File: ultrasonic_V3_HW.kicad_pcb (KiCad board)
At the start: 4 copper layers, 130 x 100 mm, 249 parts, among them J1 71918-140LF, J2 Conn_Coaxial, J3 Conn_Coaxial, J4 Conn_01x07_Pin, J5 Screw_Terminal_01x02, J6 Conn_Coaxial, J7 Conn_Coaxial, Q1 DMN6069SE, Q10 DMN6069SE, Q11 DMN6069SE, Q15 NMOS, Q2 DMN6069SE, Q3 DMN6069SE, Q4 DMN6069SE, Q5 NMOS, Q6 NMOS, Q7 DMN6069SE, Q8 DMN6069SE, Q9 DMN6069SE, U1 MACHXO2-1200HC-4TG100C, U10 MIC4604YM, U11 MIC4604YM, U12 OKI-78SR-3.3_1.5-W36H-C, U13 OKI-78SR-12_1.0-W36H-C, U15 LM34966, U17 OPA388, U18 LM393, U2 TDC_7200, U23 MCP1501-25xCH, U24 MCP1501-30xCH, U3 MAX9939, U4 TLV3501AID, U5 DGS0010A, U6 LM339, U7 ADC10065, U8 MIC4604YM, U9 MIC4604YM, X1 16MHz

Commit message: DONE - before checking
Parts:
- added R83: 12, Resistor_SMD:R_0603_1608Metric, B.Cu at (126.9, 92.0)
- added R84: 12, Resistor_SMD:R_0603_1608Metric, B.Cu at (126.9, 93.5)
- added R85: 12, Resistor_SMD:R_0603_1608Metric, B.Cu at (126.9, 95.0)
- C1, C12, C61: value 100p -> C
- C10, C11, C13, C14, C18, C20, C21, C22, C23, C24, C25, C3, C35, C38, C39, C41, C42, C44, C45, C47, C48, C50, C51, C52, C54, C63, C7, C78, C79, C8, C80, C81, C82, C83, C84, C85, C88, C89, C9: value 100n -> C
- C15, C62, C64, C65, C68, C69, C71, C73, C75, C77: value 4u7 -> C
- C16, C17, C5, C6, C66, C67, C70, C72, C74, C76, C86, C87: value 220n -> C
- C19: value 4.7u -> C
- C26, C28, C31, C32, C36, C37, C40, C43, C46, C49, C53, C60: value 1u -> C
- C27, C29, C30, C33, C4, C58: value 10n -> C
- C34, C55: value 1n -> C
- C56: value 220p -> C
- C57, C59: value 22n -> C
- D1, D2, D3, D5, D6: value 1N4148W -> D
- D24, D26, D27: value LED_GREEN -> LED
- D4: value V8PA6HM3/I -> D
- L2: value 6.8u -> L
- R1, R10, R11, R12, R13, R15, R16, R17, R18, R19, R2, R21, R24, R25, R3, R4, R51, R6, R72, R73, R74, R75, R82, R9: value 0 -> R
- R14, R23, R52, R60, R62, R63, R64, R65: value 100 -> R
- R20, R22, R26, R27, R28, R42, R43, R44, R45, R46, R47, R5, R58, R59, R61, R66, R67, R68, R69, R70, R71, R76, R77, R78, R79, R8, R80, R81: value 10k -> R
- R48: value 6k8 -> R
- R49: value 11k3 -> R
- R50: value 49k9 -> R
- R53, R54: value 10m -> R
- R7: value 1k -> R
- U19, U20, U21, U22: value ~ -> TMUX7219
- moved C14 4.82 mm to (182.7, 94.6), turned to -90 degrees
- moved C85 3.83 mm to (168.1, 69.1)
- moved R19 3.79 mm to (165.4, 92.4), turned to 0 degrees
- moved U24 3.75 mm to (167.1, 69.2), turned to 90 degrees
- moved R24 3.22 mm to (159.1, 87.6), turned to 180 degrees
- moved R15 2.81 mm to (162.4, 87.6), turned to 0 degrees
- moved R21 1.97 mm to (168.8, 92.4), turned to 0 degrees
- moved C54 1.30 mm to (165.3, 76.3)
- moved C55 1.30 mm to (165.3, 74.8)
- moved C53 1.30 mm to (165.1, 73.0)
- moved C18 1.20 mm to (165.9, 87.6)
- moved C13 0.86 mm to (156.7, 90.8), turned to 90 degrees
- moved C79 0.70 mm to (92.5, 81.3)
- moved C7 0.60 mm to (160.8, 94.1)
- moved C26 0.40 mm to (96.4, 98.2)
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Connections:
- U1 pad 10: /SPI_LOCAL_MOSI -> Net-(U1D-PL4B)
- U1 pad 12: /SPI_LOCAL_SCK -> Net-(U1D-PL5A/PCLKT3_1)
- U1 pad 9: /SPI_LOCAL_MISO -> Net-(U1D-PL4A)
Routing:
- net GND: track 253.4 -> 230.9 mm, vias 117 -> 393
- net /SPI_LOCAL_SCK: track 116.4 -> 109.2 mm, vias 5 -> 4
- net /SPI_LOCAL_MOSI: track 117.0 -> 109.9 mm, vias 4 -> 3
- net /SPI_LOCAL_MISO: track 10.9 -> 4.89 mm, vias 2 -> 1
- net Net-(U1D-PL5A/PCLKT3_1): track 0.00 -> 4.69 mm, vias 0 -> 1
- net Net-(U1D-PL4B): track 0.00 -> 4.40 mm, vias 0 -> 1
- net Net-(U1D-PL4A): track 0.00 -> 4.33 mm, vias 0 -> 1
- net Net-(U17A-+): track 12.3 -> 16.4 mm
- net /P3V_REF: track 39.6 -> 35.7 mm
- net /H-bridges/BRIDGE_CD_MUX_EN: track 82.6 -> 80.7 mm
- net /CNTRL_GPIO2: track 86.8 -> 88.5 mm, vias 2 -> 3
- net /CNTRL_GPIO3: track 33.6 -> 35.1 mm, vias 0 -> 1
- net /CNTRL_MOSI: track 47.3 -> 48.9 mm, vias 2 -> 3
- net /CNTRL_GPIO1: track 33.8 -> 35.0 mm, vias 0 -> 1
- net /CNTRL_SCLK: track 49.1 -> 50.3 mm, vias 2 -> 3
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- added copper zone on B.Cu, net GND
- added copper zone on F.Cu, net GND

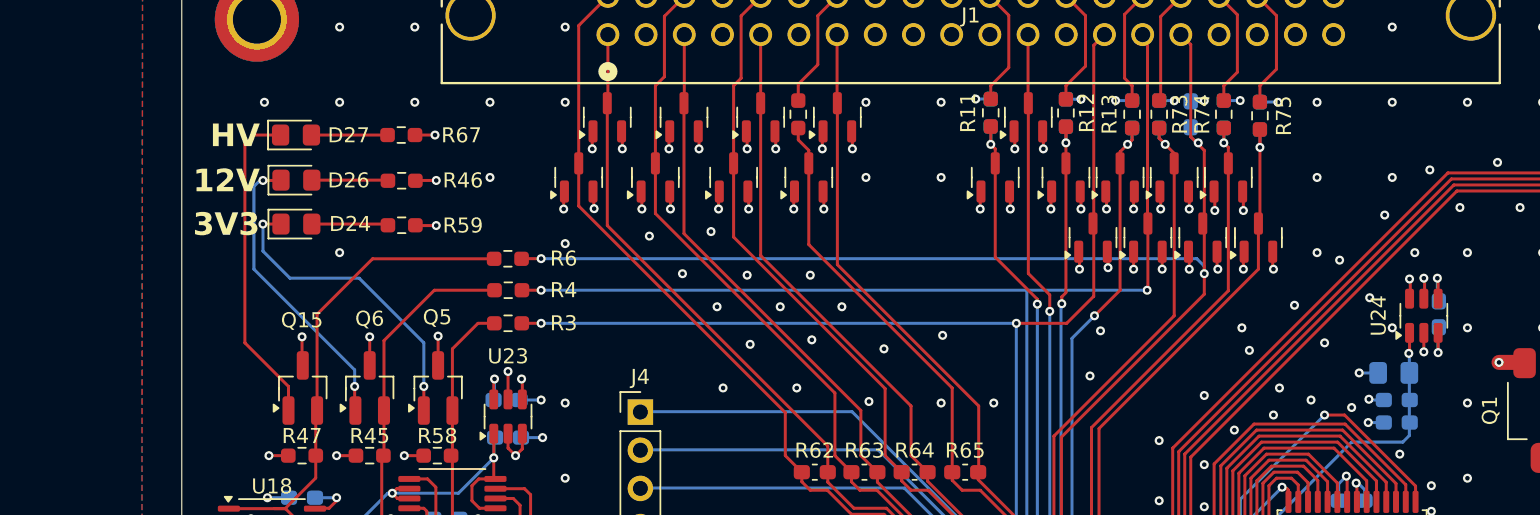
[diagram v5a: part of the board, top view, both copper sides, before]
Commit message: most values in schematic filled corrected footprint mistake
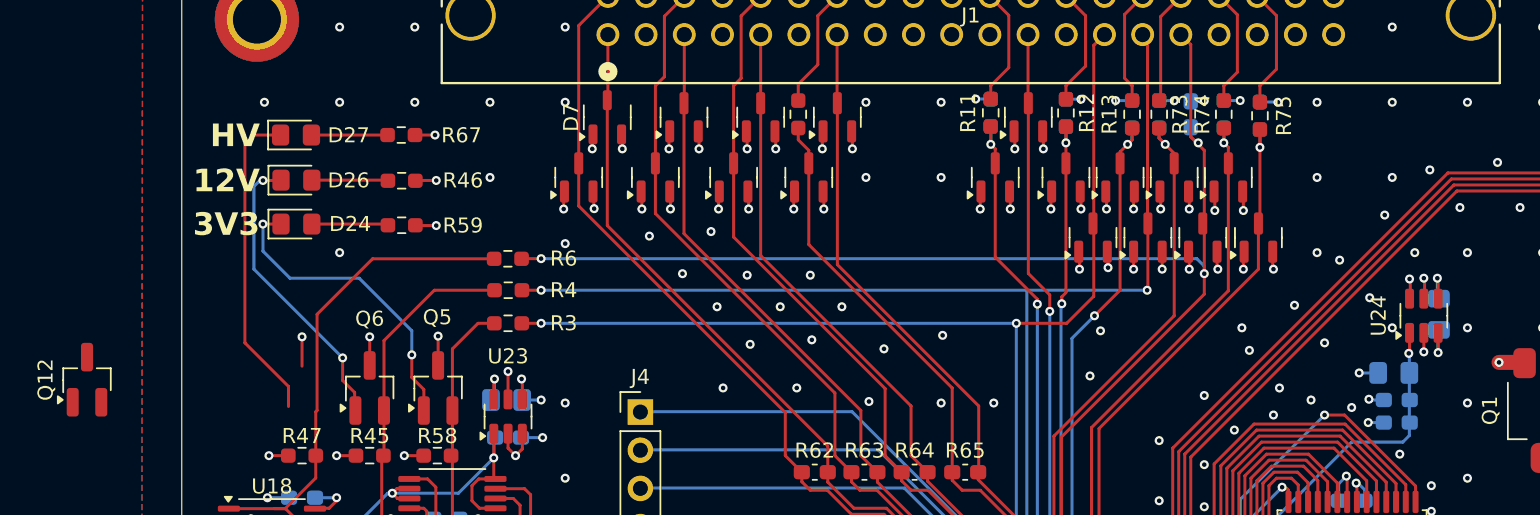
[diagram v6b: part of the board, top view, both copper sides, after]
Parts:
- removed Q15: NMOS, Package_TO_SOT_SMD:SOT-23_Handsoldering
- added Q12: Q_NMOS_GSD, Package_TO_SOT_SMD:SOT-23_Handsoldering, F.Cu at (78.2, 73.5)
- C1, C12, C61: value C -> 100p
- C10, C11, C53, C60: value C -> 1u
- C13, C14, C27, C29, C30, C33, C54, C58, C63, C7, C78, C79, C80, C89, C9: value C -> 100n
- C15, C26, C28, C31, C32, C62: value C -> 10u
- C55: value C -> 10n
- C56: value C -> 220p
- C57: value C -> 22n
- C59: value C -> 220n
- C85, C88: value C -> 1u; footprint Capacitor_SMD:C_0603_1608Metric_Pad1.08x0.95mm_HandSolder -> Capacitor_SMD:C_0805_2012Metric_Pad1.18x1.45mm_HandSolder
- D4: value D -> V8PA6HM3/I
- D7: footprint Package_TO_SOT_SMD:SOT-23 -> Package_TO_SOT_SMD:SOT-23-3
- L2: value L -> 6.8u
- Q5, Q6: value NMOS -> Q_NMOS_GSD
- R11, R12, R13, R18, R3, R4, R51, R6, R72, R73, R74, R75, R82: value R -> 0
- R16, R17, R19, R21, R46, R59, R67: value R -> 1k
- R22: value R -> 8k2
- R45, R47, R5, R58, R8: value R -> 10k
- R48: value R -> 24k9
- R49: value R -> 11k3
- R50: value R -> 49k9
- R52: value R -> 100
- R53, R54: value R -> 10m
- R7: value R -> 10
- U5: value DGS0010A -> DAC60501
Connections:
- Q5 pad 1: Net-(D24-K) -> /P_GOOD_P3V3
- Q5 pad 2: /P_GOOD_P3V3 -> GND
- Q5 pad 3: GND -> Net-(D24-K)
- Q6 pad 1: Net-(D26-K) -> /P_GOOD_P12V
- Q6 pad 2: /P_GOOD_P12V -> GND
- Q6 pad 3: GND -> Net-(D26-K)
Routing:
- net GND: track 230.9 -> 227.0 mm, vias 393 -> 391
- net Net-(D26-K): track 19.4 -> 21.3 mm, vias 2 -> 3
- net Net-(D24-K): track 20.5 -> 22.4 mm, vias 2 -> 3
